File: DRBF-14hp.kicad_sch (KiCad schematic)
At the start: 98 parts, among them J1 VER-A, J10 INV-A, J11 INV-B, J2 In-A, J3 In-AB, J4 In-B, J5 Eurorack_Power, J6 VER-B, J7 Out-A, J8 Out-AB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

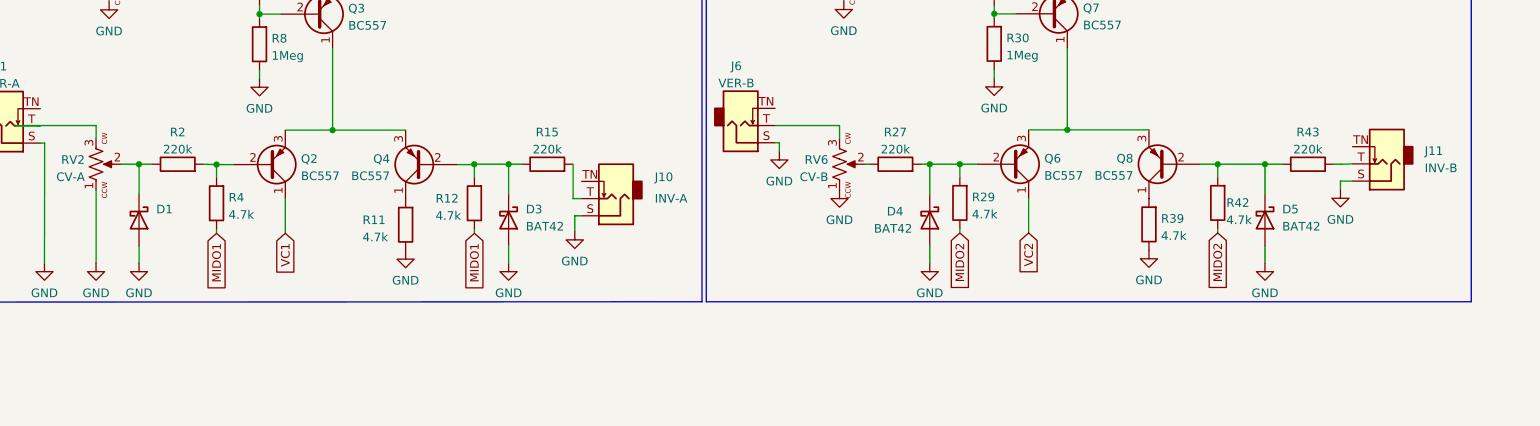
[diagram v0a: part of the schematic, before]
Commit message: Changed to 14hp width
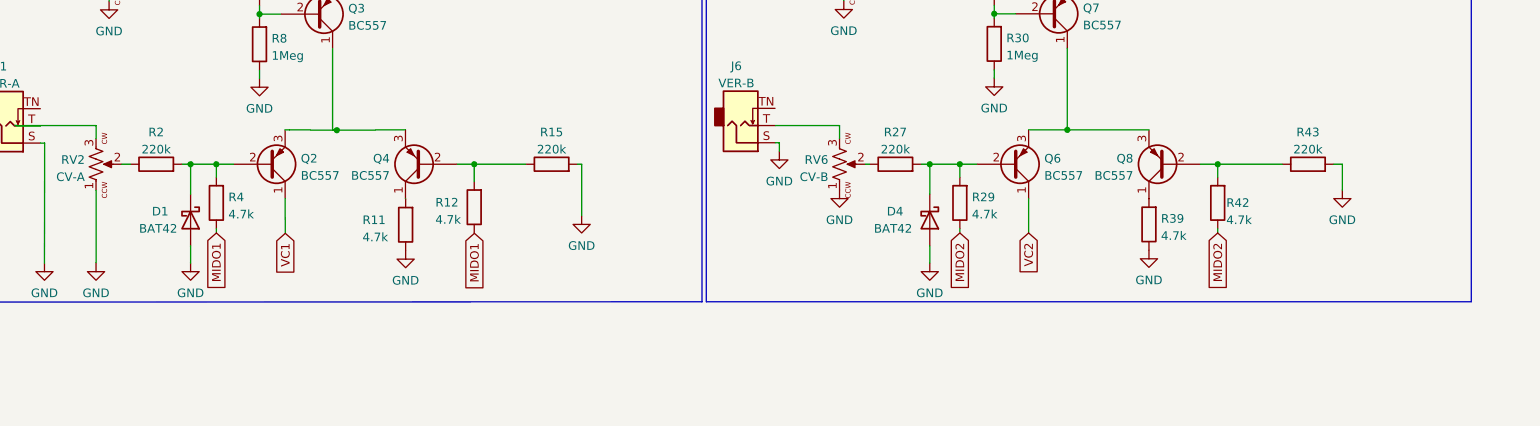
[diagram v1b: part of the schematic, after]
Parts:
- removed D3, D5: BAT42, Diode_THT:D_DO-35_SOD27_P7.62mm_Horizontal, symbol Diode:BAT42
- removed J10: INV-A, winterbloom:AudioJack_WQP518MA, symbol winterbloom:Eurorack_Mono_Jack
- removed J11: INV-B, winterbloom:AudioJack_WQP518MA, symbol winterbloom:Eurorack_Mono_Jack
- D1: value (none) -> BAT42; footprint (none) -> Diode_THT:D_DO-35_SOD27_P7.62mm_Horizontal
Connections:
- net GND: now also R15.2, R43.2
- net at R15.1: now also Q4.2 (B), R12.2
- net at R2.1, RV2.2: no longer D1.1 (K)
- net at Q2.2 (B), R2.2, R4.2: now also D1.1 (K)
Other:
- moved on the sheet: D1, R12, R15, R2
